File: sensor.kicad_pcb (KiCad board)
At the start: 2 copper layers, 38.7 x 42.8 mm, 13 parts, among them J1 Conn_01x06, U1 TCR2EF19, U2 PMW3610

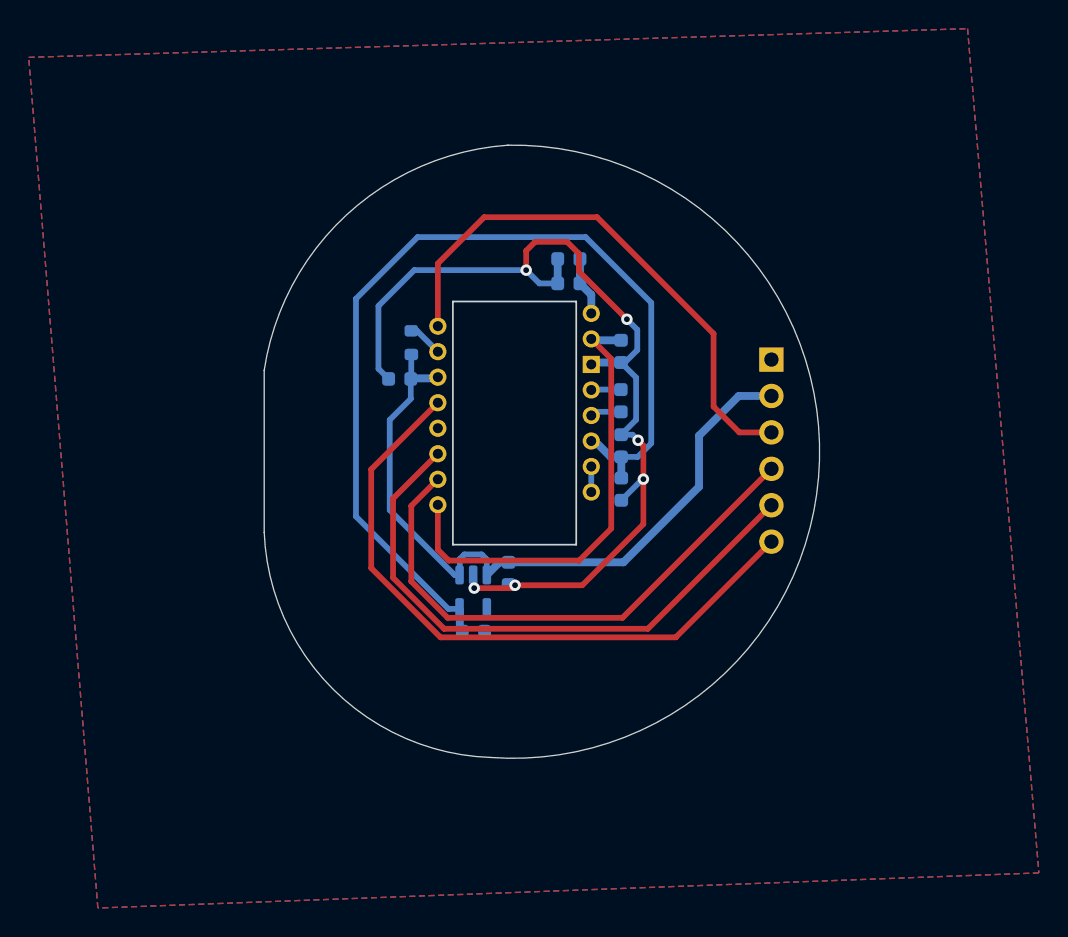
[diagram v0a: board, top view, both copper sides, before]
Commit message: updated design
- updated spi pinout suitable for use with ribbon cables and the charybdis mcu holder
- updated ibom to reflect pinout changes
- gerbers and relevant smt files moved to production dir
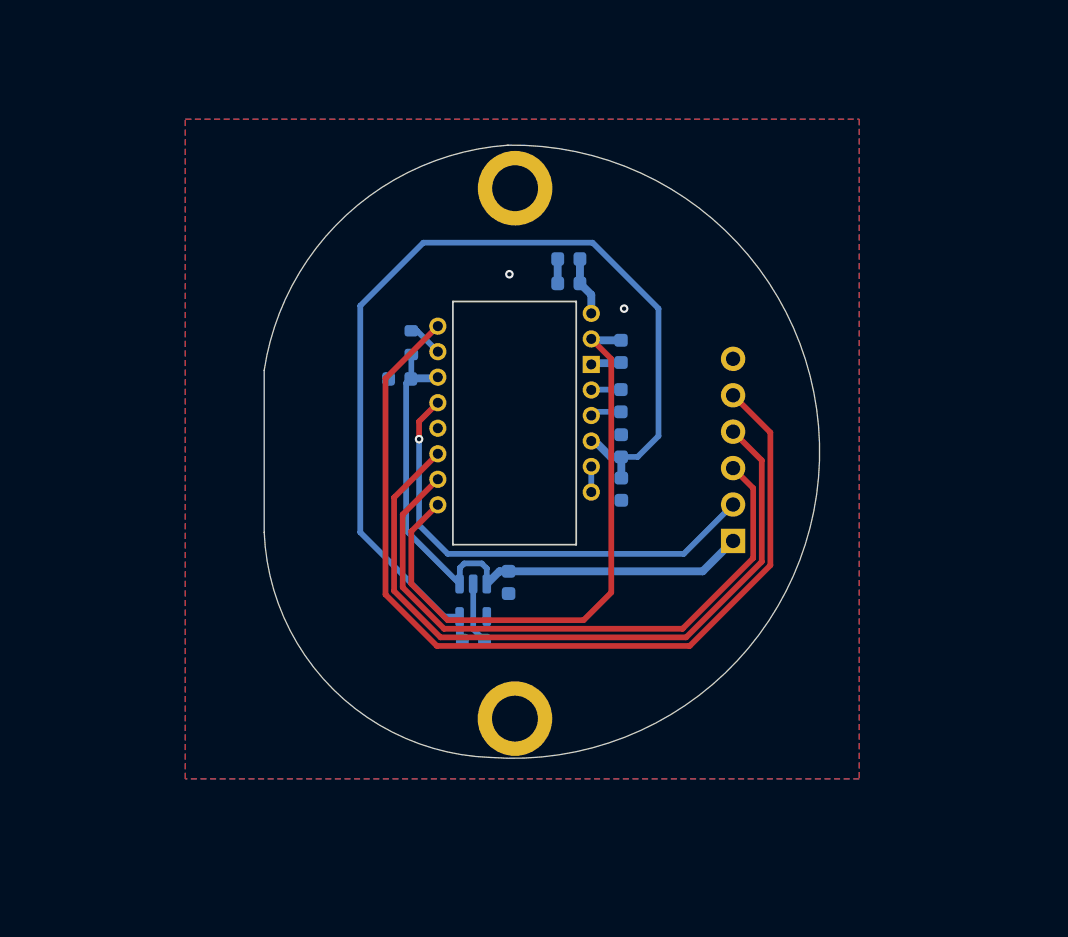
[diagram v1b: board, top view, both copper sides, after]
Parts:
- added ?: , , F.Cu at (81.6, 129.2)
- added REF**: MountingHole_3.2mm_M3_ISO7380_Pad, MountingHole:MountingHole_3.2mm_M3_ISO7380_Pad, F.Cu at (81.6, 92.2)
- moved J1 12.9 mm to (96.8, 116.8), turned to 180 degrees
- moved C4 0.63 mm to (81.1, 119.7)
- moved C5 0.63 mm to (78.7, 123.7)
- moved U1 0.63 mm to (78.7, 120.9)
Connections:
- J1 pad 1: GND -> VCC
- J1 pad 2: VCC -> NCS_2
- J1 pad 3: MOTION_2 -> SDIO_2
- J1 pad 4: SDIO_2 -> SCLK_2
- J1 pad 5: SCLK_2 -> MOTION_2
- J1 pad 6: NCS_2 -> GND
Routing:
- net GND: track 68.8 -> 8.12 mm, vias 6 -> 2
- net MOTION_2: track 38.2 -> 63.8 mm
- net NCS_2: track 46.1 -> 33.2 mm, vias 0 -> 1
- net Net-(C1-Pad1): track 32.2 -> 42.3 mm
- net VCC: track 50.6 -> 41.4 mm
- net SCLK_2: track 41.4 -> 49.9 mm
- net SDIO_2: track 38.4 -> 43.1 mm
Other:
- board text added: "github.com/ufan 2022.09.04 voided 2023.03.16"
- board text removed: "github.com/ufan 2022.09.04"

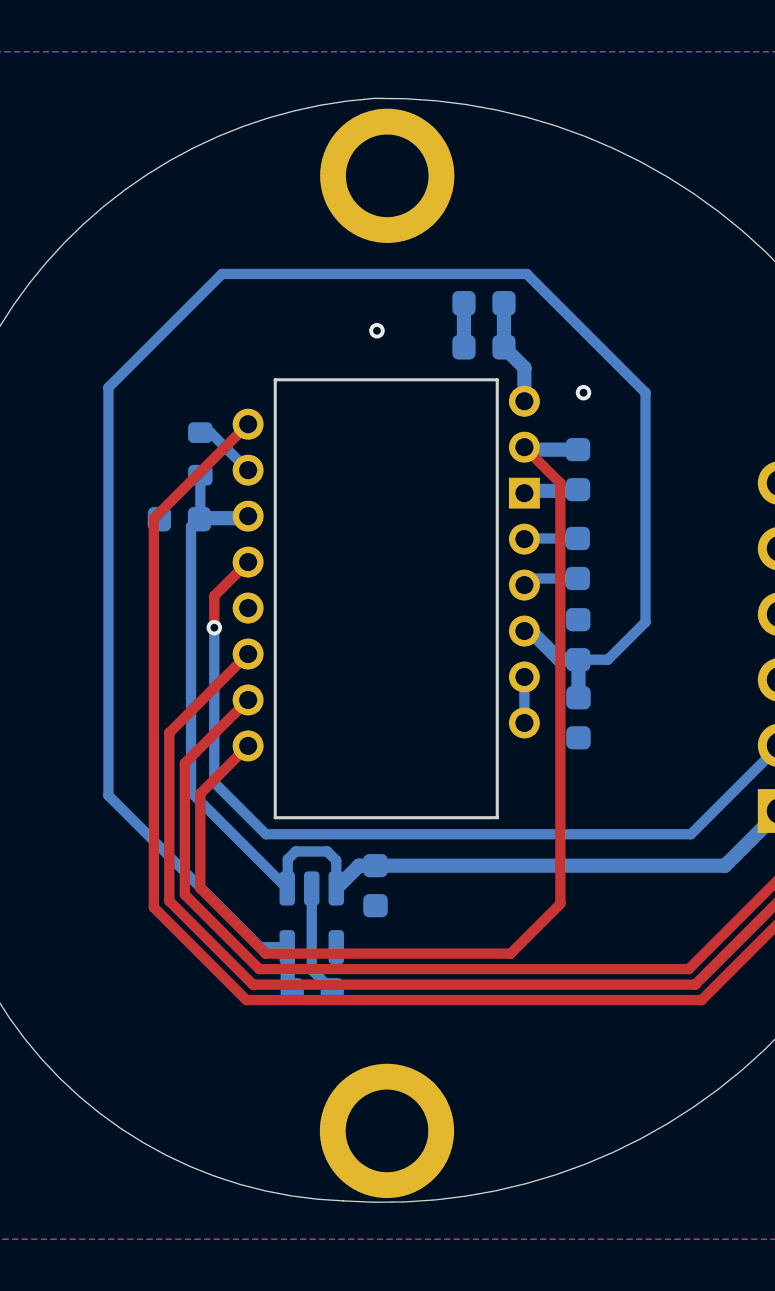
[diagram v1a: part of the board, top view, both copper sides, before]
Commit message: updated schematic
- updated spi pinout to reflect pcb changes
- added mounting holes
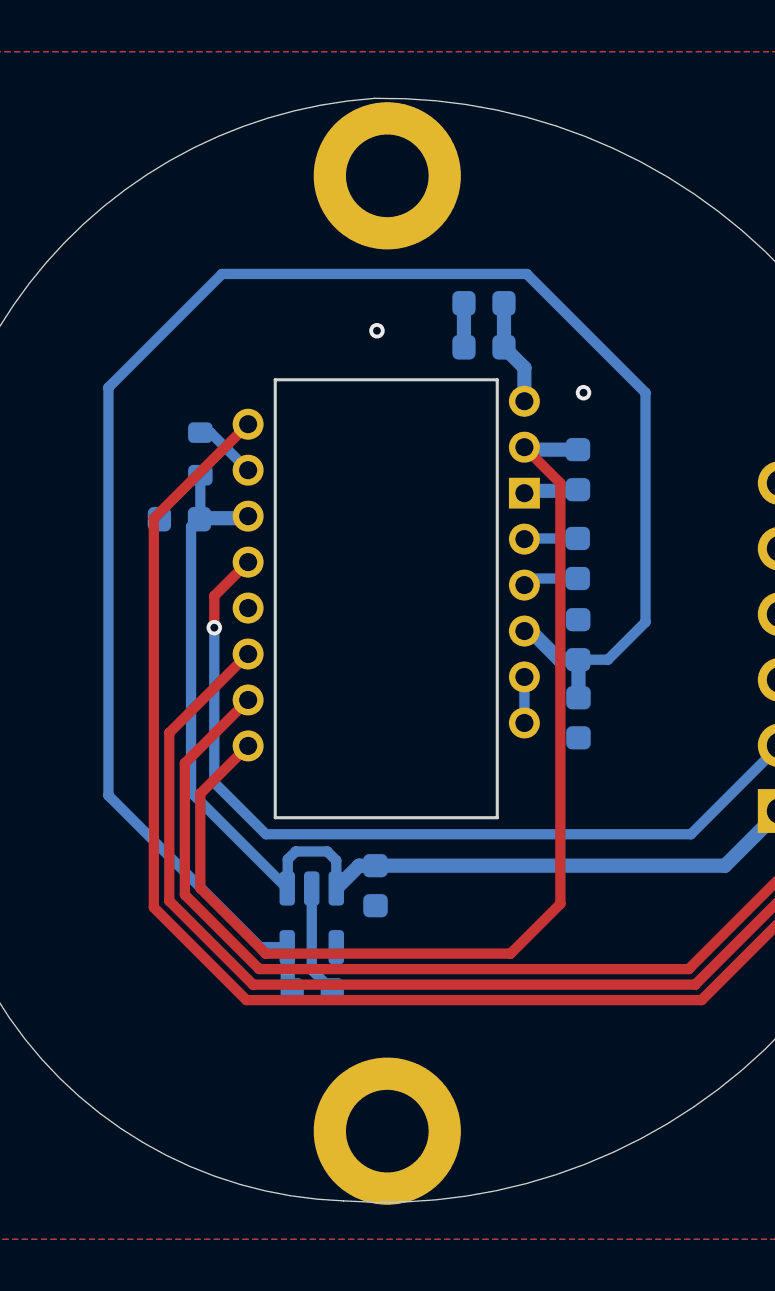
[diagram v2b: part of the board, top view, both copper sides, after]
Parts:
- removed ?: , 
- removed REF**: MountingHole_3.2mm_M3_ISO7380_Pad, MountingHole:MountingHole_3.2mm_M3_ISO7380_Pad
- added H1: MountingHole, MountingHole:MountingHole_3.2mm_M3_ISO7380_Pad, F.Cu at (81.6, 92.2)
- added H2: MountingHole, MountingHole:MountingHole_3.2mm_M3_ISO7380_Pad, F.Cu at (81.6, 129.2)

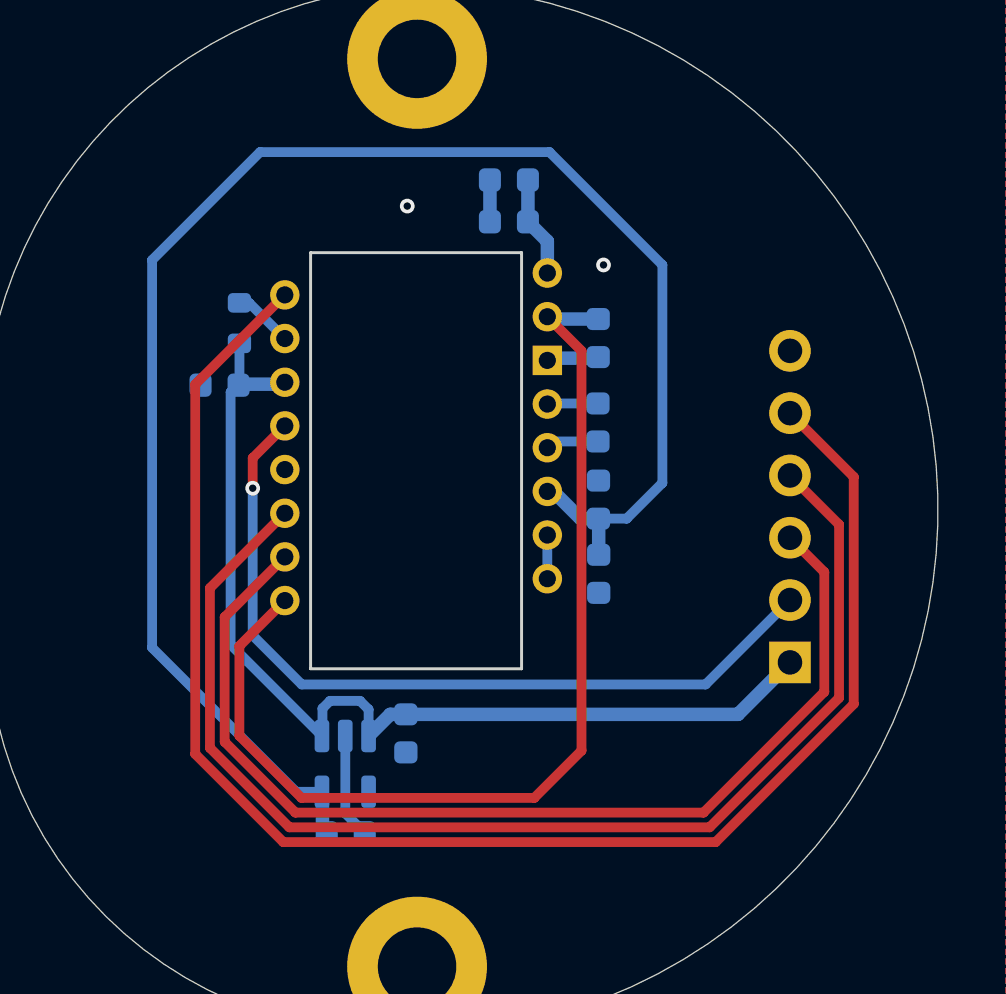
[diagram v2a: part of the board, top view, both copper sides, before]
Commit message: breakout update
- updated out of spec capacitors from schematic/bom to match reference design
- updated voltage regulator
- updated nets
- updated pinout silkscreen to match mcu holder
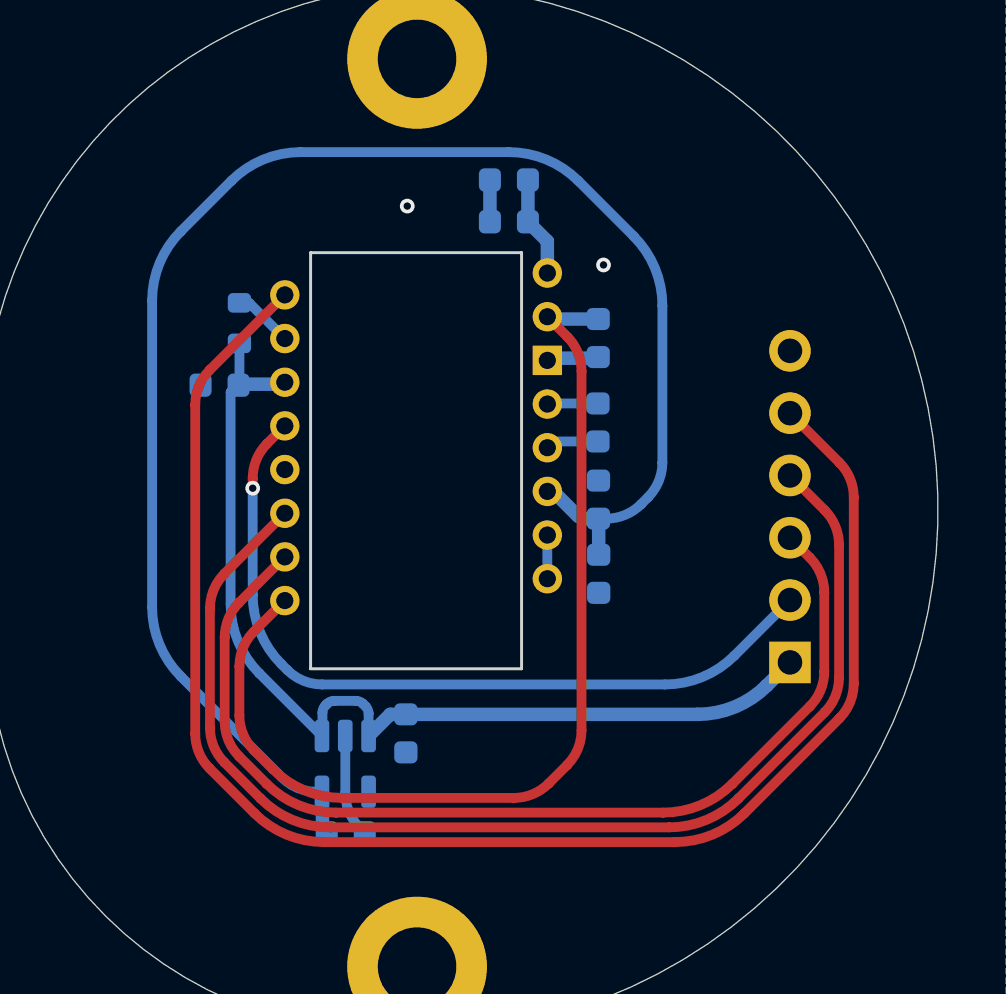
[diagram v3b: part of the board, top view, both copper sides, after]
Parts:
- C4: value 0.1u -> 1u
- C6: value 100n (X7R) -> 100n (X7R)
- C8: value 10u (X7R) -> 10u (X7R)
- C9: value 10n (X7R) -> 10n (X7R)
- U1: value TCR2EF19 -> TLV74318PDBVR
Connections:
- net +1V9 renamed +1V8
- net MOTION_2 renamed MOTION
- net NCS_2 renamed NCS
- net SCLK_2 renamed SCLK
- net SDIO_2 renamed SDIO
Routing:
- net +1V8: track 66.9 -> 65.7 mm
- net SCLK: track 49.9 -> 49.1 mm
- net MOTION: track 63.8 -> 63.1 mm
- net SDIO: track 43.1 -> 42.3 mm
- net Net-(U2-+VCSEL): track 42.3 -> 41.6 mm
- net NCS: track 33.2 -> 32.7 mm
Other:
- board text added: "CS"
- board text added: "MISO"
- board text added: "MOSI"
- board text removed: "MOTION"
- board text removed: "NCS"
- board text removed: "SDIO"
